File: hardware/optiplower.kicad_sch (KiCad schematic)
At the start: 22 parts, among them J1 Conn_01x02, J2 Conn_01x03, U1 LR7533-M, U2 XL4015, U3 DS2502, U4 ATtiny25-10SSU, U5 ATtiny85-20PU, U6 DS2502S+

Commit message: Make design completely SMD
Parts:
- removed C6: 470uF, Optiplower:CP_Radial_D8.0mm_P3.50mm_H11.5, symbol Device:C_Polarized
- removed U3: DS2502, Package_TO_SOT_THT:TO-92_Inline, symbol Optiplower:DS2502
- removed U5: ATtiny85-20PU, Package_DIP:DIP-8_W7.62mm, symbol MCU_Microchip_ATtiny:ATtiny85-20P
- added C1: 22uF, Capacitor_SMD:C_0805_2012Metric_Pad1.18x1.45mm_HandSolder, symbol Device:C
- added C3, C7, C8: 220uF, Capacitor_SMD:CP_Elec_6.3x7.7, symbol Device:C_Polarized
- C2: value 470uF -> 220uF; footprint Optiplower:CP_Radial_D8.0mm_P3.50mm_H11.5 -> Capacitor_SMD:CP_Elec_6.3x7.7; LCSC C88730 -> C340768; MPN 25PX470MEFC8X11.5 -> UCM1E221MCL1GS; Manufacturer Rubycon -> Nichicon
- J1: now fitted
- J2: footprint Connector_PinHeader_1.27mm:PinHeader_1x05_P1.27mm_Vertical -> Optiplower:Output_pads
- U3: renamed from U4; now fitted
- renumbered C1 to C10, C3 to C4, C4 to C5, C5 to C6, C7 to C9, U6 to U1, U1 to U4
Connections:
- net +24V: now also C3.1
- net GND: now also C3.2, C7.2, C8.2
- net VCC: now also C7.1, C8.1
- no-connect marks 10 -> 5

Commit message: Add ATTiny to BOM
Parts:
- U3: now in the parts list
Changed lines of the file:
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@@
   )
   (symbol (lib_id "MCU_Microchip_ATtiny:ATtiny25-20SS") (at 142.24 97.79 0) (unit 1)
-    (in_bom no) (on_board yes) (dnp no) (fields_autoplaced)
+    (in_bom yes) (on_board yes) (dnp no) (fields_autoplaced)
     (property "Reference" "U3" (at 128.27 97.155 0)
       (effects (font (size 1.27 1.27)) (justify right))

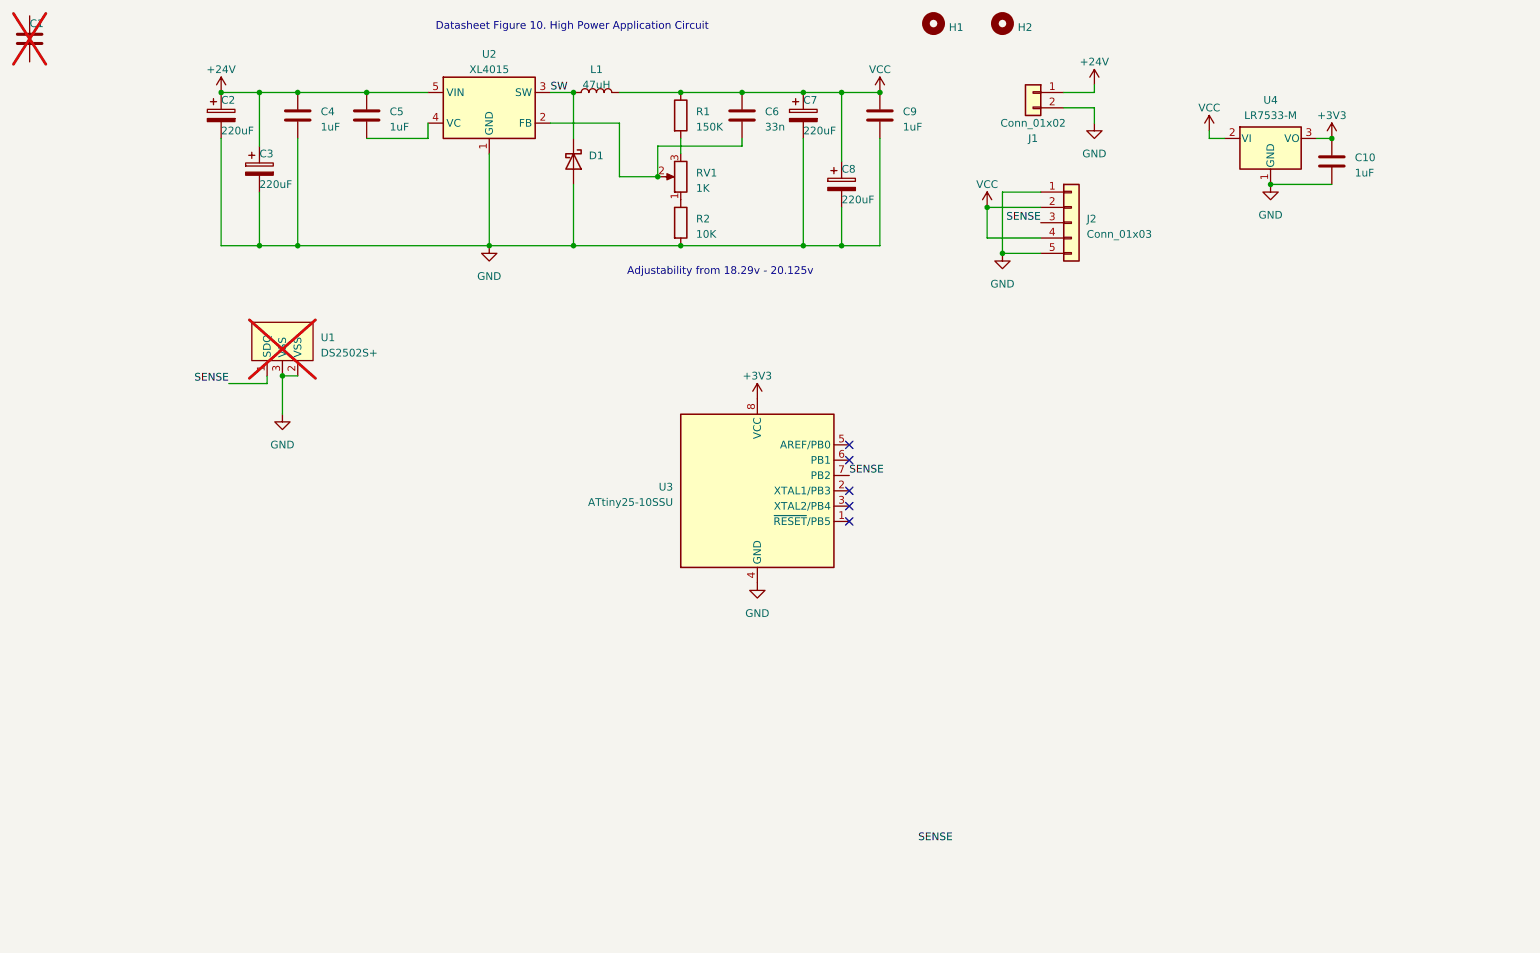
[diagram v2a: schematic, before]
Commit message: Relayout so caps fit in gap
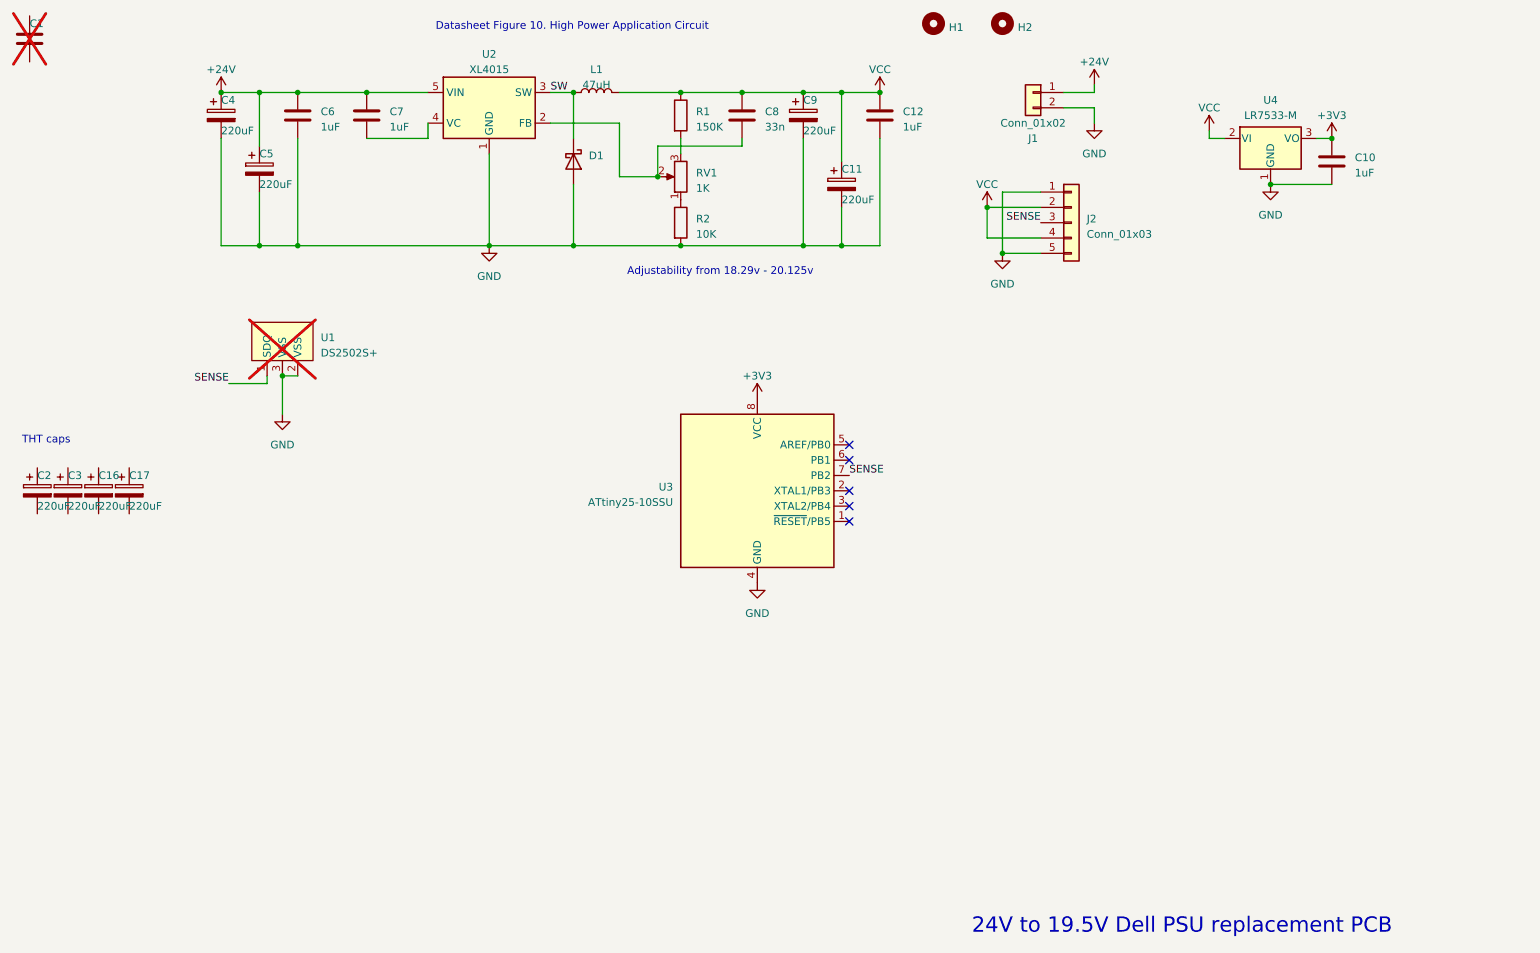
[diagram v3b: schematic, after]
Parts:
- removed C7, C8: 220uF, Capacitor_SMD:CP_Elec_6.3x7.7, symbol Device:C_Polarized
- added C11, C4, C5, C9: 220uF, Capacitor_SMD:CP_Elec_6.3x7.7, symbol Device:C_Polarized
- added C16, C17: 220uF, Capacitor_THT:C_Radial_D6.3mm_H11.0mm_P2.50mm, symbol Device:C_Polarized
- C2, C3: footprint Capacitor_SMD:CP_Elec_6.3x7.7 -> Capacitor_THT:C_Radial_D6.3mm_H11.0mm_P2.50mm; LCSC C340768 -> C402586; MPN UCM1E221MCL1GS -> GH221M025E110A; Manufacturer Nichicon -> Capxon International Elec; now left out of the parts list
- renumbered C9 to C12, C4 to C6, C5 to C7, C6 to C8
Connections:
- net +24V: now also C4.1, C5.1; no longer C2.1, C3.1
- net GND: now also C11.2, C4.2, C5.2, C9.2; no longer C2.2, C3.2
- net VCC: now also C11.1, C9.1
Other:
- note added: "24V to 19.5V Dell PSU replacement PCB"
- note added: "THT caps"
- moved on the sheet: C2
